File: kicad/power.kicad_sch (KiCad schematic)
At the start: 7 parts, among them U1 LM1117DT-3.3, U2 TME-0505S, U4 R-78B3.3-1.0 (Recom)

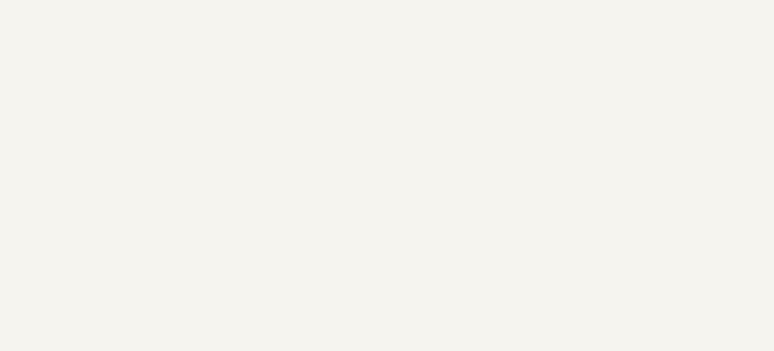
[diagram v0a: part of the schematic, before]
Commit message: Fixed power issue
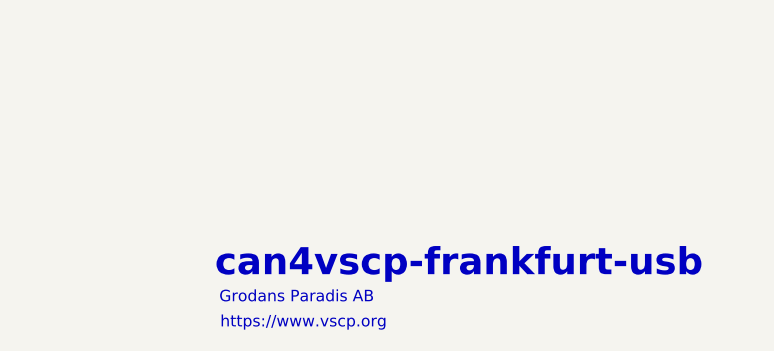
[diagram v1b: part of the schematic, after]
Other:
- note added: "Grodans Paradis AB"
- note added: "can4vscp-frankfurt-usb"
- note added: "https://www.vscp.org"
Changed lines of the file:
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@@
+		)
+	)
+	(text "can4vscp-frankfurt-usb"
+		(exclude_from_sim no)
+		(at 207.518 170.434 0)
+		(effects
+			(font
+				(size 3 3)
+				(thickness 0.6)
+				(bold yes)
+			)
 		)
 	)
@@
 		)
 	)
+	(text "https://www.vscp.org"
+		(exclude_from_sim no)
+		(at 190.246 177.038 0)
+		(effects
+			(font
+				(size 1.27 1.27)
+			)
+		)
+	)
 	(text "Alternativ 2"
 		(exclude_from_sim no)
@@
 		(effects
 			(font
+				(size 1.27 1.27)
+			)
+		)
+	)
+	(text "Grodans Paradis AB"
+		(exclude_from_sim no)
+		(at 189.484 174.244 0)
+		(effects
+			(font

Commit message: Reversion A schema and PCB
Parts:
- removed C10: 1uF, Capacitor_SMD:C_0805_2012Metric_Pad1.18x1.45mm_HandSolder, symbol Device:CP_Small
- removed C9: 10uF, Capacitor_SMD:C_0805_2012Metric_Pad1.18x1.45mm_HandSolder, symbol Device:CP_Small
- removed U1: LM1117DT-3.3, Package_TO_SOT_SMD:TO-252-3_TabPin2, symbol Regulator_Linear:LM1117DT-3.3
- removed U4: R-78B3.3-1.0 (Recom), Converter_DCDC:Converter_DCDC_RECOM_R-78B-2.0_THT, symbol Regulator_Switching:R-78B3.3-2.0
- added IC4: NCP1117-1.5_SOT223, Package_TO_SOT_SMD:SOT-223-3_TabPin2, symbol Regulator_Linear:NCP1117-1.5_SOT223
- C7, C8: footprint Capacitors_SMD:C_0805 -> Capacitor_SMD:C_0805_2012Metric
- renumbered U2 to IC5
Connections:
- net +5V: now also IC4.3 (VI)
- net GND: now also IC4.1 (GND)
- net +3V3 renamed +3.3V
- net +3.3V: now also IC4.2 (VO)
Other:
- note removed: "Alternativ 2"
- note removed: "Alternative 1"
- moved on the sheet: C7, C8, IC5
